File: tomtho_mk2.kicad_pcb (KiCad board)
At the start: 2 copper layers, 275.8 x 106.3 mm, 179 parts, among them J1 USB-C, J2 BATTERY, J3 TRACKPAD, Q1 AO3401A, SW1 SKRAAWE010, SW10 SKRAAWE010, SW11 SKRAAWE010, SW12 SKRAAWE010, SW13 SKRAAWE010, SW14 SKRAAWE010, SW15 SKRAAWE010, SW16 SKRAAWE010, SW17 SKRAAWE010, SW18 SKRAAWE010, SW19 SKRAAWE010, SW2 SKRAAWE010, SW20 SKRAAWE010, SW21 SKRAAWE010, SW22 SKRAAWE010, SW23 SKRAAWE010, SW24 SKRAAWE010, SW25 SKRAAWE010, SW26 SKRAAWE010, SW27 SKRAAWE010, SW28 SKRAAWE010, SW29 SKRAAWE010, SW3 SKRAAWE010, SW30 SKRAAWE010, SW31 SKRAAWE010, SW32 SKRAAWE010, SW33 SKRAAWE010, SW34 SKRAAWE010, SW35 SKRAAWE010, SW36 SKRAAWE010, SW37 SKRAAWE010, SW38 SKRAAWE010, SW39 SKRAAWE010, SW4 SKRAAWE010, SW40 SKRAAWE010, SW41 SKRAAWE010, SW42 SKRAAWE010, SW43 SKRAAWE010, SW44 SKRAAWE010, SW45 SKRAAWE010, SW46 SKRAAWE010, SW47 SKRAAWE010, SW48 SKRAAWE010, SW49 SKRAAWE010, SW5 SKRAAWE010, SW50 SKRAAWE010, SW51 SKRAAWE010, SW52 SKRAAWE010, SW53 SKRAAWE010, SW54 SKRAAWE010, SW55 SKRAAWE010, SW56 SKRAAWE010, SW57 SKRAAWE010, SW58 SKRAAWE010, SW59 SKRAAWE010, SW6 SKRAAWE010, SW60 SKRAAWE010, SW61 SKRAAWE010, SW62 SKRAAWE010, SW63 SKRAAWE010, SW64 SKRAAWE010, SW65 SKRAAWE010, SW66 RESET, SW67 POWER, SW7 SKRAAWE010, SW8 SKRAAWE010, SW9 SKRAAWE010, U1 MDBT50Q-1MV2, U2 USBLC6-2SC6, U3 MCP73831

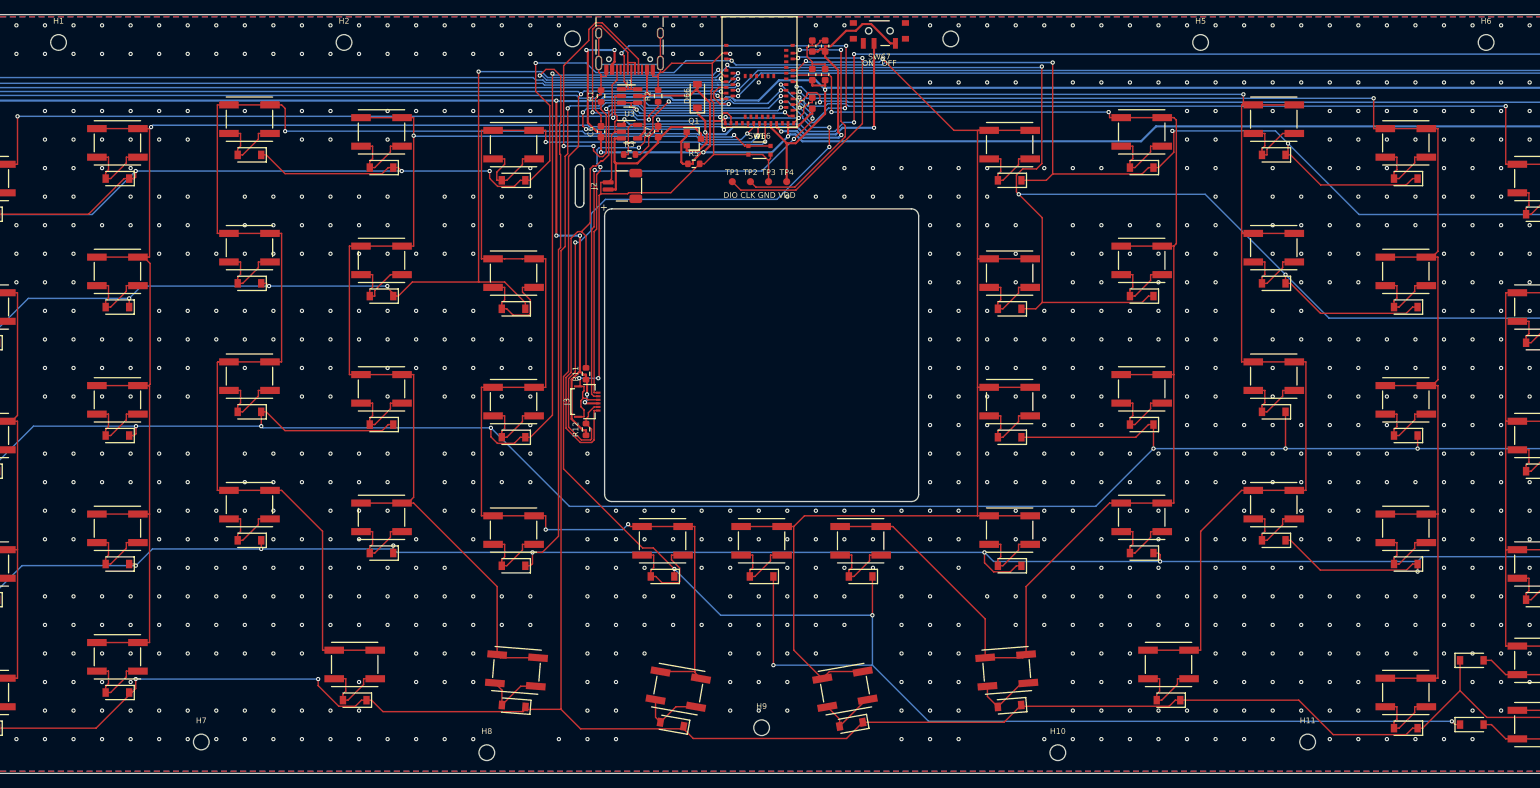
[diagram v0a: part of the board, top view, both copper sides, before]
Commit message: Ashiyu: screwless case - skirt down to the desk, bottom tray inside with 8 hidden spring clips; PCB floats on 8 Tadpole D3.0 pins (4 rear, 2 front, 2 centre); PCB holes d3.1 (DRC 0/0/0)
Co-Authored-By: Claude Opus 5.5 <noreply@anthropic.com>
Claude-Session: https://claude.ai/code/session_014QKLhpB6tKWk1p8Y7v384p
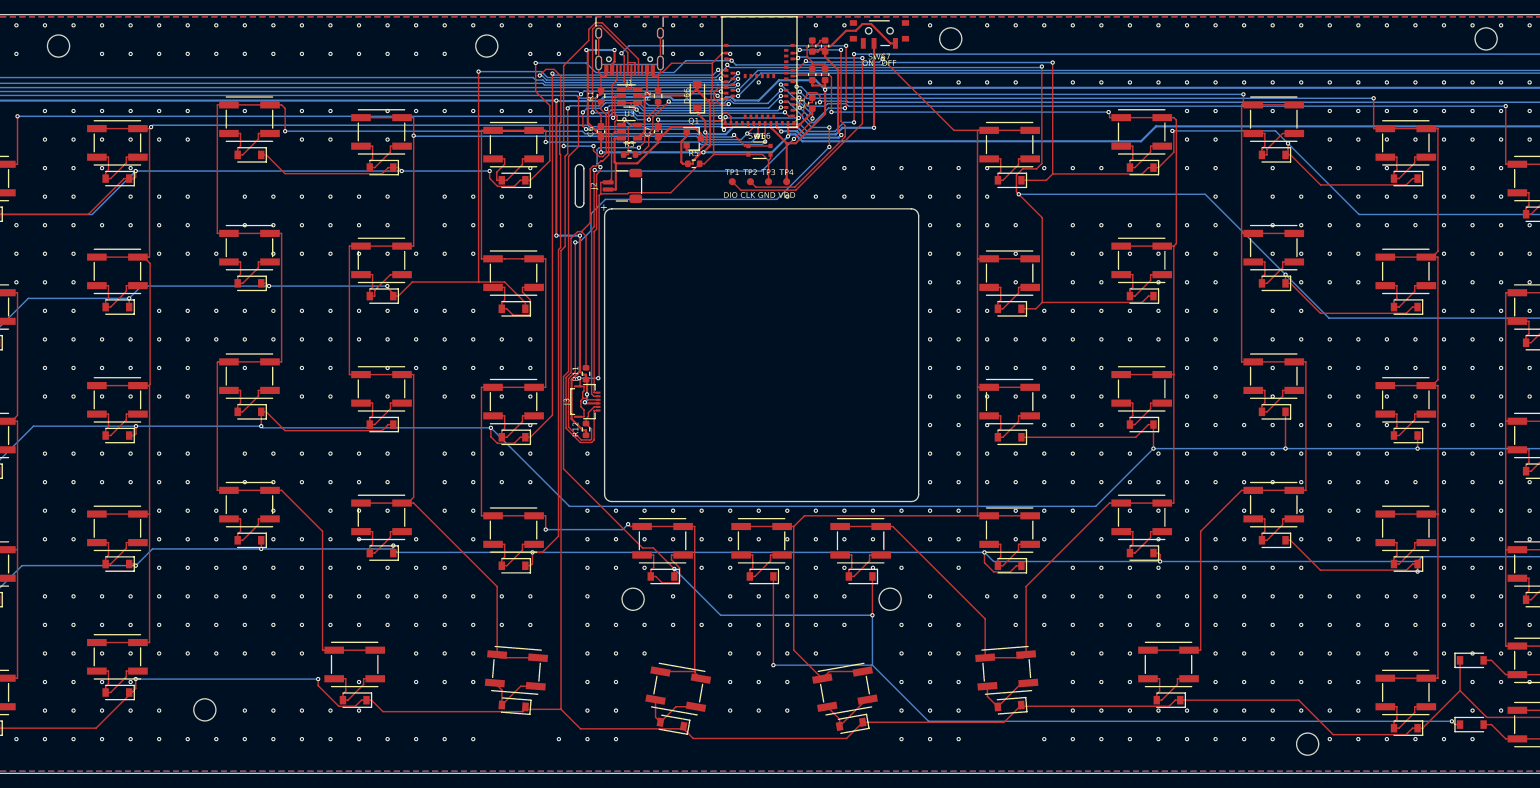
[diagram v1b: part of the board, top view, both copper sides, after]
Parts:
- removed H10, H11, H9: M2, tomtho_mk2:MountingHole_2.2mm_M2
- H1, H2, H3, H4, H5, H6, H7, H8: value M2 -> Tadpole; footprint tomtho_mk2:MountingHole_2.2mm_M2 -> tomtho_mk2:Tadpole_D3.0_NPTH
- moved H5 167.9 mm to (60.5, 98.0)
- moved H6 101.4 mm to (215.0, 102.8)
- moved H4 75.0 mm to (240.0, 4.00)
- moved H7 63.7 mm to (120.5, 82.5)
- moved H8 60.5 mm to (156.5, 82.5)
- moved H3 53.0 mm to (165.0, 4.00)
- moved H2 20.0 mm to (100.0, 5.00)
- moved H1 0.50 mm to (40.0, 5.00)
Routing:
- net GND: vias 1174 -> 1164

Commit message: Ashiyu v22: lower-left Ctrl 1u / Fn+Win 0.5u stacked / Alt 1u (66 keys, Win on ROW5 COL1); 9th Tadpole pin (front centre); trackpad without cover plate (module touched directly through a 41x38 window, 1.0x0.5 lip); 1.5 mm top chamfer; refs SW101/SW102/D101; re-routed (Freerouting 1.9, local check 0 errors); case CI reads case_inputs from the PCB via pcbnew; HANDOFF.md
Co-Authored-By: Claude Opus 5.5 <noreply@anthropic.com>
Claude-Session: https://claude.ai/code/session_01Rq3DZsqPhBbL1FAX1XrxAC
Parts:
- removed SW67: POWER, tomtho_mk2:SW_SPDT_PCM12
- added D101: B5819W, tomtho_mk2:D_SOD-123, F.Cu at (129.5, 12.0)
- added H9: Tadpole, tomtho_mk2:Tadpole_D3.0_NPTH, F.Cu at (138.5, 100.5)
- added SW101: RESET, tomtho_mk2:SW_TS-1928-B, F.Cu at (138.2, 19.6)
- added SW102: POWER, tomtho_mk2:SW_SPDT_PCM12, F.Cu at (155.0, 3.20)
- D66: value B5819W -> 1N4148W
- SW66: value RESET -> SKRAAWE010; footprint tomtho_mk2:SW_TS-1928-B -> tomtho_mk2:SW_ALPS_SKRA_6.2mm
- moved D66 139.7 mm to (238.0, 100.1), turned to 0 degrees
- moved SW66 135.5 mm to (247.2, 100.1)
- moved SW62 98.3 mm to (29.8, 100.1)
- moved SW65 98.3 mm to (152.4, 74.3)
- moved D62 88.1 mm to (39.0, 100.1), turned to 0 degrees
- moved D65 88.1 mm to (152.4, 79.3), turned to 180 degrees
- moved D63 13.9 mm to (124.6, 79.3)
- moved D64 13.9 mm to (138.5, 79.3)
- moved SW63 13.9 mm to (124.6, 74.3)
- moved SW64 13.9 mm to (138.5, 74.3)
- moved D50 13.3 mm to (39.0, 91.1), turned to 0 degrees
- moved D51 4.99 mm to (48.2, 100.6)
- moved SW51 4.99 mm to (48.2, 95.6)
- moved SW50 4.50 mm to (29.8, 91.1)
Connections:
- D62 pad 2: /K5_5 -> /K5_1
- D63 pad 2: /K5_6 -> /K5_5
- D64 pad 2: /K5_7 -> /K5_6
- D65 pad 2: /K5_10 -> /K5_7
- D66 pad 1: /VSYS -> /ROW5
- D66 pad 2: /VBUS -> /K5_10
- SW62 pad 1: /COL5 -> /COL1
- SW62 pad 2: /K5_5 -> /K5_1
- SW63 pad 1: /COL6 -> /COL5
- SW63 pad 2: /K5_6 -> /K5_5
- SW64 pad 1: /COL7 -> /COL6
- SW64 pad 2: /K5_7 -> /K5_6
- SW65 pad 1: /COL10 -> /COL7
- SW65 pad 2: /K5_10 -> /K5_7
- SW66 pad 1: /RESET -> /COL10
- SW66 pad 2: GND -> /K5_10
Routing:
- net /COL1: track 221.0 -> 296.5 mm
- net /ROW2: track 424.5 -> 350.5 mm, vias 10 -> 2
- net /VDD: track 356.2 -> 426.5 mm, vias 8 -> 10
- net /ROW1: track 400.3 -> 337.6 mm, vias 10 -> 4
- net /ROW0: track 376.4 -> 318.2 mm, vias 11 -> 2
- net /ROW3: track 413.2 -> 359.5 mm, vias 11 -> 2
- net /RESET: track 59.7 -> 11.8 mm, vias 4 -> 2
- net /COL10: track 234.1 -> 278.6 mm, vias 2 -> 4
- net /ROW5: track 356.6 -> 395.0 mm, vias 7 -> 4
- net /LED_PWR_R: track 137.4 -> 171.1 mm, vias 2 -> 3
- net /CC1: track 43.3 -> 15.0 mm, vias 2 -> 0
- net /ROW4: track 392.1 -> 414.5 mm, vias 4 -> 2
- net /COL6: track 177.2 -> 199.2 mm, vias 2 -> 6
- net /VDDH: track 38.1 -> 55.5 mm
- net /TP_SCL: track 90.6 -> 74.5 mm
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
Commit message: PCB: drop 2 unused escape vias (LED_BT1, LED_PWR_R) flagged as via_dangling by DRC
Co-Authored-By: Claude Opus 5.5 <noreply@anthropic.com>
Claude-Session: https://claude.ai/code/session_01Rq3DZsqPhBbL1FAX1XrxAC
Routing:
- net /LED_BT1: track 124.6 -> 123.4 mm, vias 1 -> 0
- net /LED_PWR_R: track 171.1 -> 170.0 mm, vias 3 -> 2
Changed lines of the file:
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@@
 	(gr_arc (start 160.5 67.812) (mid 160.2071 68.5191) (end 159.5 68.812) (stroke (width 0.1) (type default)) (layer "Edge.Cuts"))
 	(gr_arc (start 117.5 68.812) (mid 116.7929 68.5191) (end 116.5 67.812) (stroke (width 0.1) (type default)) (layer "Edge.Cuts"))
-	(segment (start 134.45 8.8) (end 135.2 8.8) (width 0.2) (layer "F.Cu") (net 83))
 	(segment (start 134.45 9.6) (end 135.2 9.6) (width 0.2) (layer "F.Cu") (net 85))
 	(segment (start 134.45 10.4) (end 135.2 10.4) (width 0.2) (layer "F.Cu") (net 87))
 	(segment (start 134.45 11.2) (end 135.2 11.2) (width 0.2) (layer "F.Cu") (net 90))
-	(segment (start 134.45 12) (end 135.2 12) (width 0.2) (layer "F.Cu") (net 92))
 	(segment (start 141.95 13.6) (end 141.2 13.6) (width 0.2) (layer "F.Cu") (net 107))
 	(segment (start 141.95 12.8) (end 141.2 12.8) (width 0.2) (layer "F.Cu") (net 106))
@@
 	(segment (start 18.097 10.471) (end 16.727 9.1) (width 0.2) (layer "F.Cu") (net 83))
 	(segment (start 16.075 9.1) (end 16.727 9.1) (width 0.2) (layer "F.Cu") (net 83))
-	(segment (start 134.816 8.8) (end 135.2 8.8) (width 0.2) (layer "F.Cu") (net 83))
 	(segment (start 134.45 8.8) (end 134.816 8.8) (width 0.2) (layer "F.Cu") (net 83))
 	(segment (start 14.425 9.1) (end 14.425 8.373) (width 0.2) (layer "F.Cu") (net 84))
@@
 	(segment (start 201.416 13.615) (end 149.24 13.615) (width 0.2) (layer "F.Cu") (net 92))
 	(segment (start 149.24 13.615) (end 149.068 13.787) (width 0.2) (layer "F.Cu") (net 92))
-	(segment (start 134.825 12) (end 135.2 12) (width 0.2) (layer "F.Cu") (net 92))
 	(segment (start 134.45 12) (end 134.825 12) (width 0.2) (layer "F.Cu") (net 92))
 	(segment (start 270.2 9.925) (end 270.2 9.273) (width 0.2) (layer "F.Cu") (net 93))
@@
 	(segment (start 128 18.95) (end 128.752 18.95) (width 0.3) (layer "F.Cu") (net 114))
 	(segment (start 129.5 13.65) (end 129.5 13.988) (width 0.3) (layer "F.Cu") (net 114))
-	(via (at 135.2 8.8) (size 0.6) (drill 0.3) (layers "F.Cu" "B.Cu") (net 83))
 	(via (at 135.2 9.6) (size 0.6) (drill 0.3) (layers "F.Cu" "B.Cu") (net 85))
 	(via (at 135.2 10.4) (size 0.6) (drill 0.3) (layers "F.Cu" "B.Cu") (net 87))
 	(via (at 135.2 11.2) (size 0.6) (drill 0.3) (layers "F.Cu" "B.Cu") (net 90))
-	(via (at 135.2 12) (size 0.6) (drill 0.3) (layers "F.Cu" "B.Cu") (net 92))
 	(via (at 141.2 13.6) (size 0.6) (drill 0.3) (layers "F.Cu" "B.Cu") (net 107))
 	(via (at 141.2 12.8) (size 0.6) (drill 0.3) (layers "F.Cu" "B.Cu") (net 106))
